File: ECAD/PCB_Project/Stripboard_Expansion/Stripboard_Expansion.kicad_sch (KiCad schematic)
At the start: 9 parts, among them J1 Inductive, J2 Ultrasonic, J3 Conn_01x03, J4 LDR, J5 LED, J6 MCU, J8 Conn_01x04

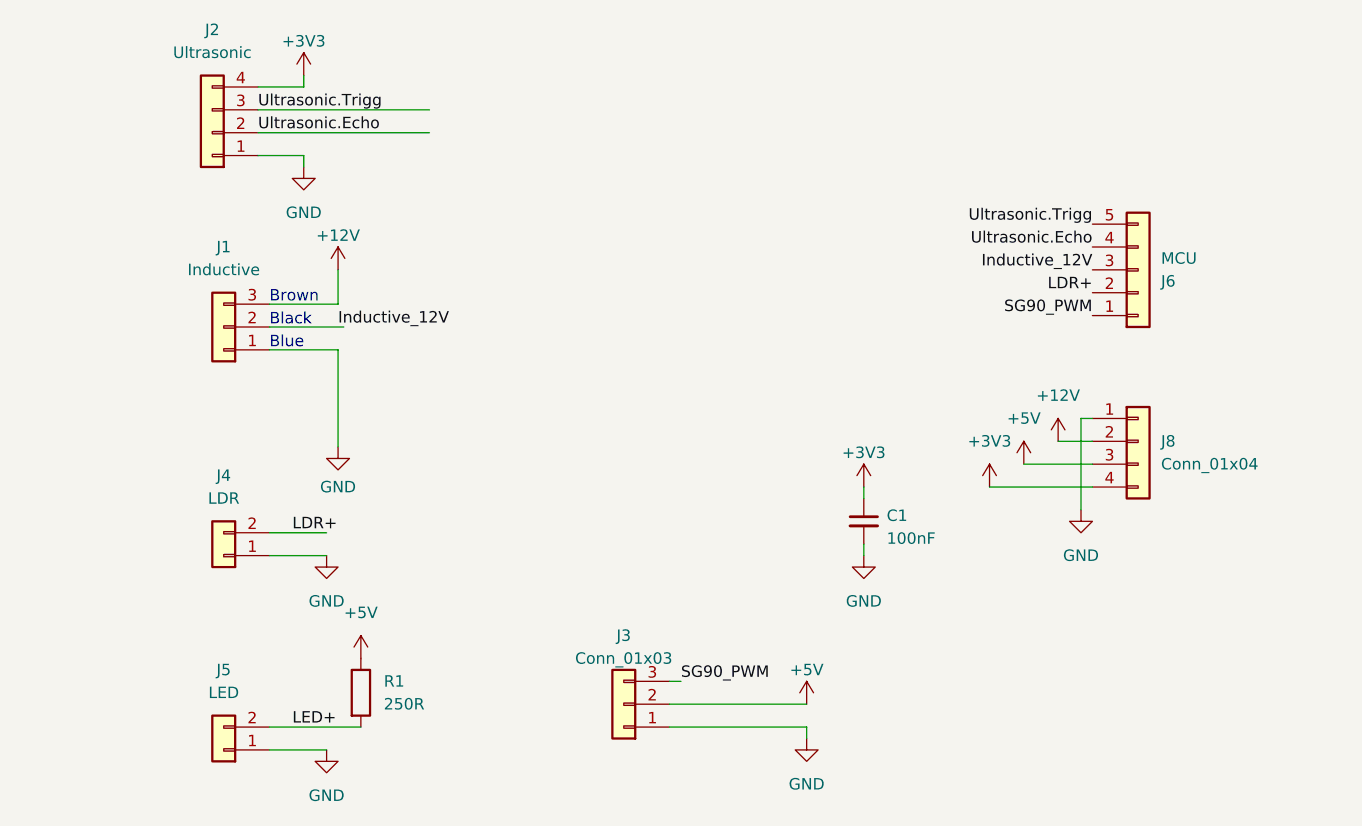
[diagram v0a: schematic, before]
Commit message: Pushing
COde changes:
MP driver under development
SG90 as well

PCB:
final version, as sent to manufacture

Sims
New sims for report.
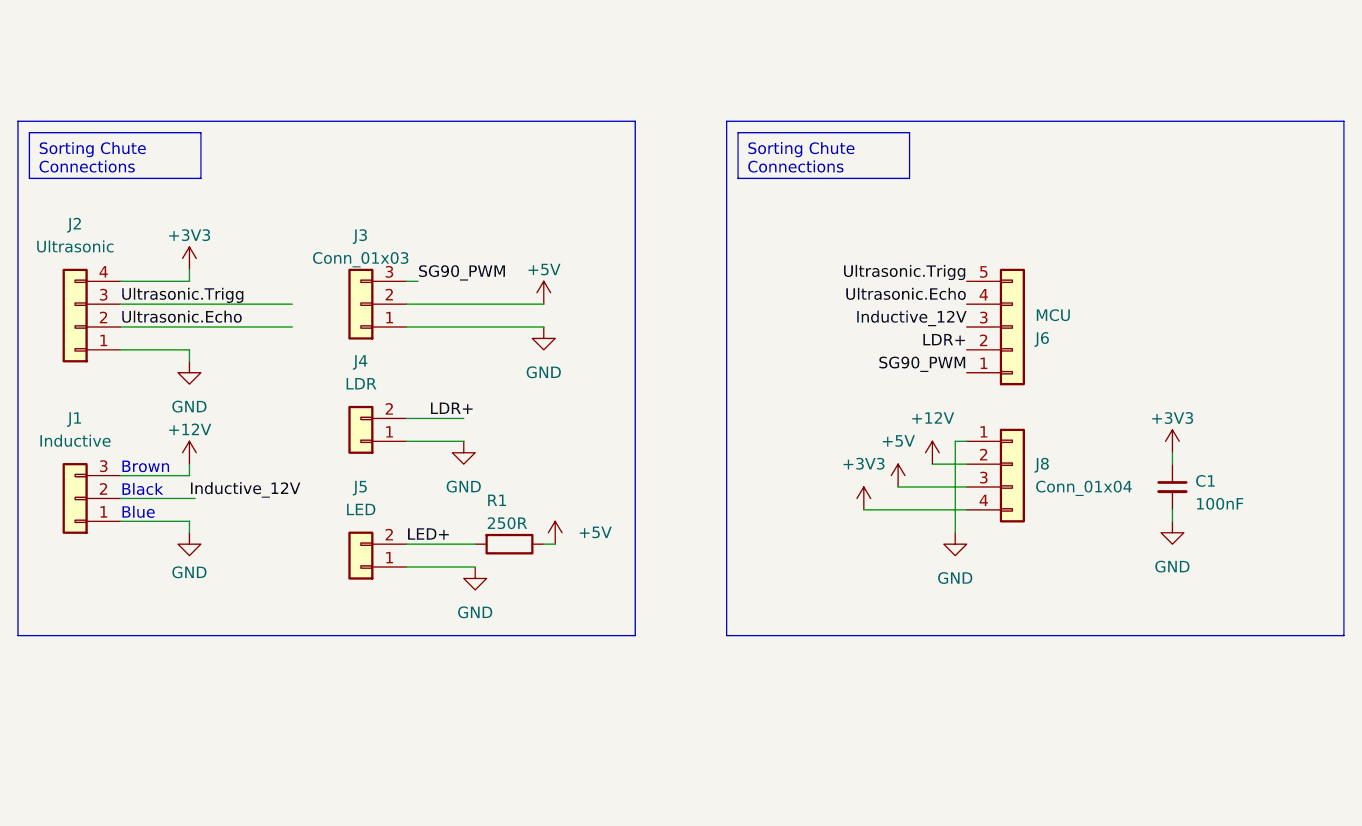
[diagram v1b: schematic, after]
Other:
- moved on the sheet: C1, J1, J2, J3, J4, J5, J6, J8, R1
